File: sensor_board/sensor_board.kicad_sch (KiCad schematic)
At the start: 11 parts, among them J2 Conn_01x05_Pin, U2 LTC4316IMS-PBF

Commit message: sensor board
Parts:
- removed JP1, JP2: SolderJumper_2_Open, symbol Jumper:SolderJumper_2_Open
- removed R3: R_LT, symbol Device:R
- removed R4, R5, R6: R, symbol Device:R
- removed R7: R_HT, symbol Device:R
- removed U2: LTC4316IMS-PBF, MSOP-10_MS_LIT, symbol LTC4316:LTC4316IMS-PBF
- added C3, C4: 0.1uF, symbol Device:C
- added C5: 10uF, symbol Device:C
- added RT2: NTCLE203E3103GB0, NTCLE203E3103GB0, symbol NTCLE203E3103GB0:NTCLE203E3103GB0
- added U1: TSL25911FN, SON-06-FN_2000X2400_AMS, symbol TSL25911:TSL25911FN
- R1: value R_LB -> 1k
- R2: value R_HB -> 5.6k
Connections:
- net +3V3: now also R1.2, C3.2, C4.2, C5.1, RT2.2, U1.5 (VDD)
- net GND: now also R2.2, C3.1, C5.2; no longer R1.1, R2.1
- net SCL: now also J2.5 (Pin_5), U1.1 (SCL)
- net SDA: now also J2.4 (Pin_4), U1.6 (SDA)
- net VOUT: now also R2.1, RT2.1
- new net: R1.1, U1.2 (INT)
- new net: C4.1, U1.3 (GND)

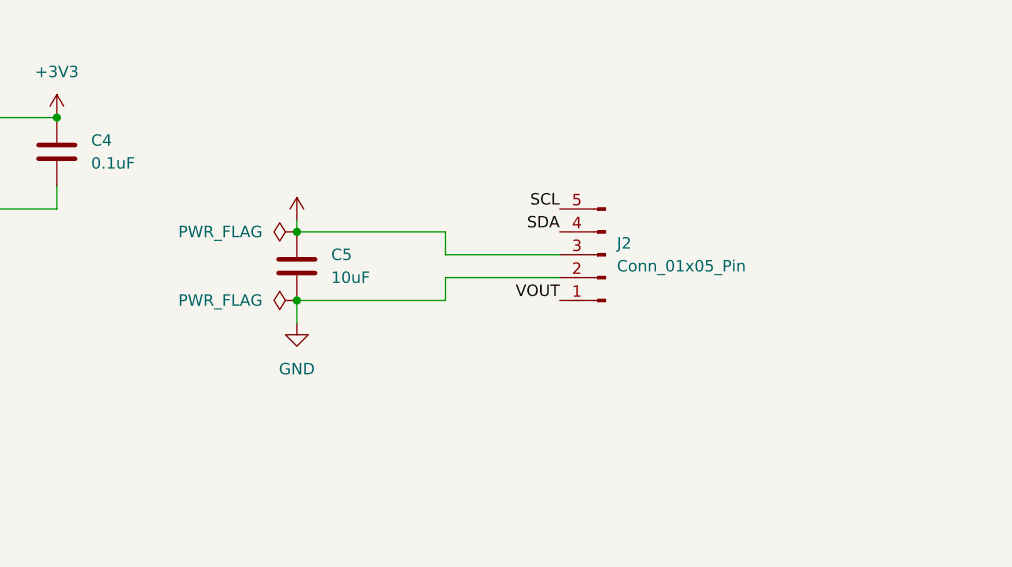
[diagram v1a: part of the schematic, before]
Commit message: added more complexity + thermistor connection
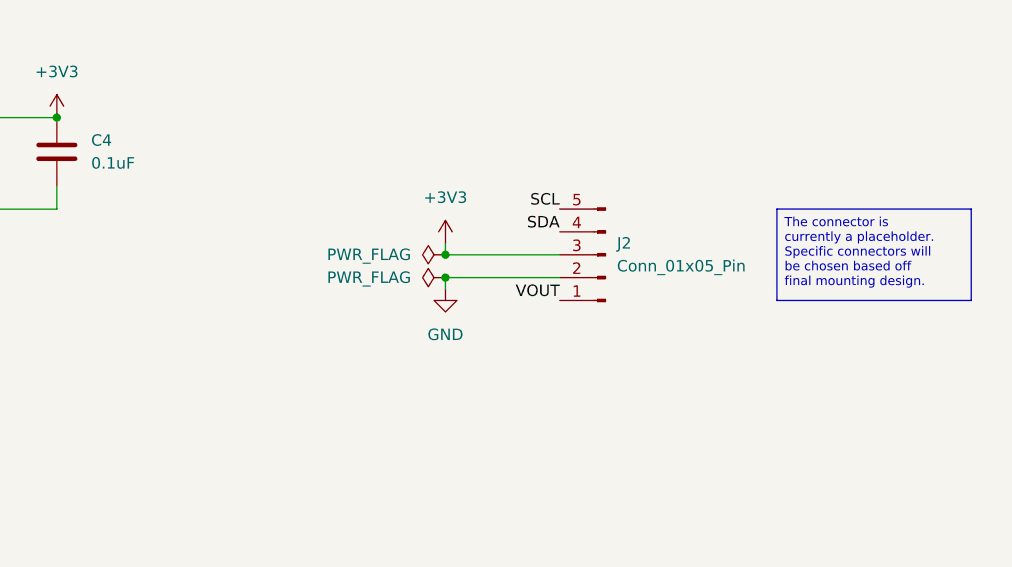
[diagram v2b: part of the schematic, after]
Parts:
- removed C5: 10uF, symbol Device:C

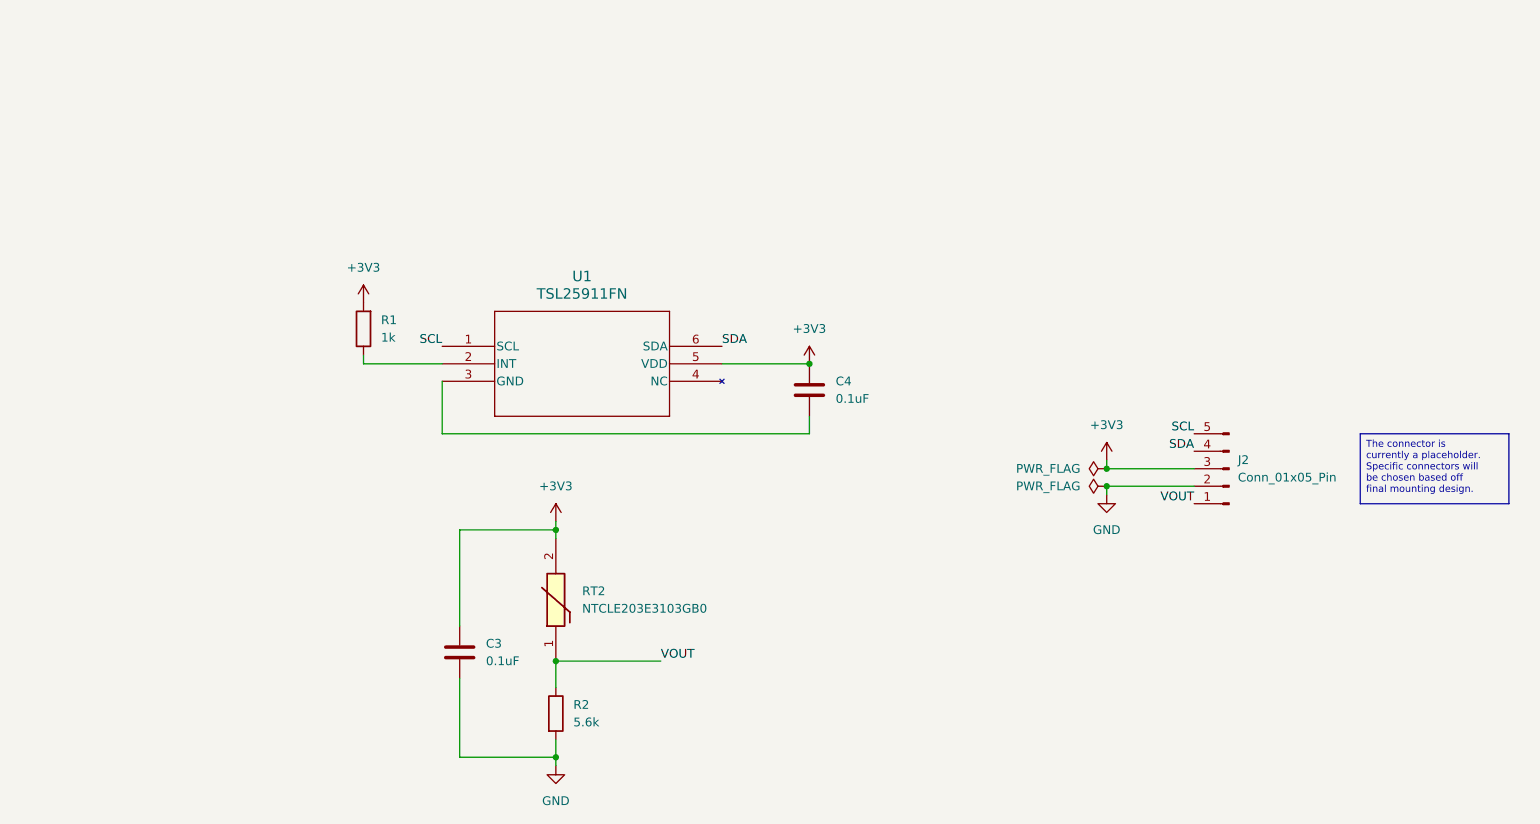
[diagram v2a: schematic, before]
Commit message: Initial version of sensor communication through all three boards
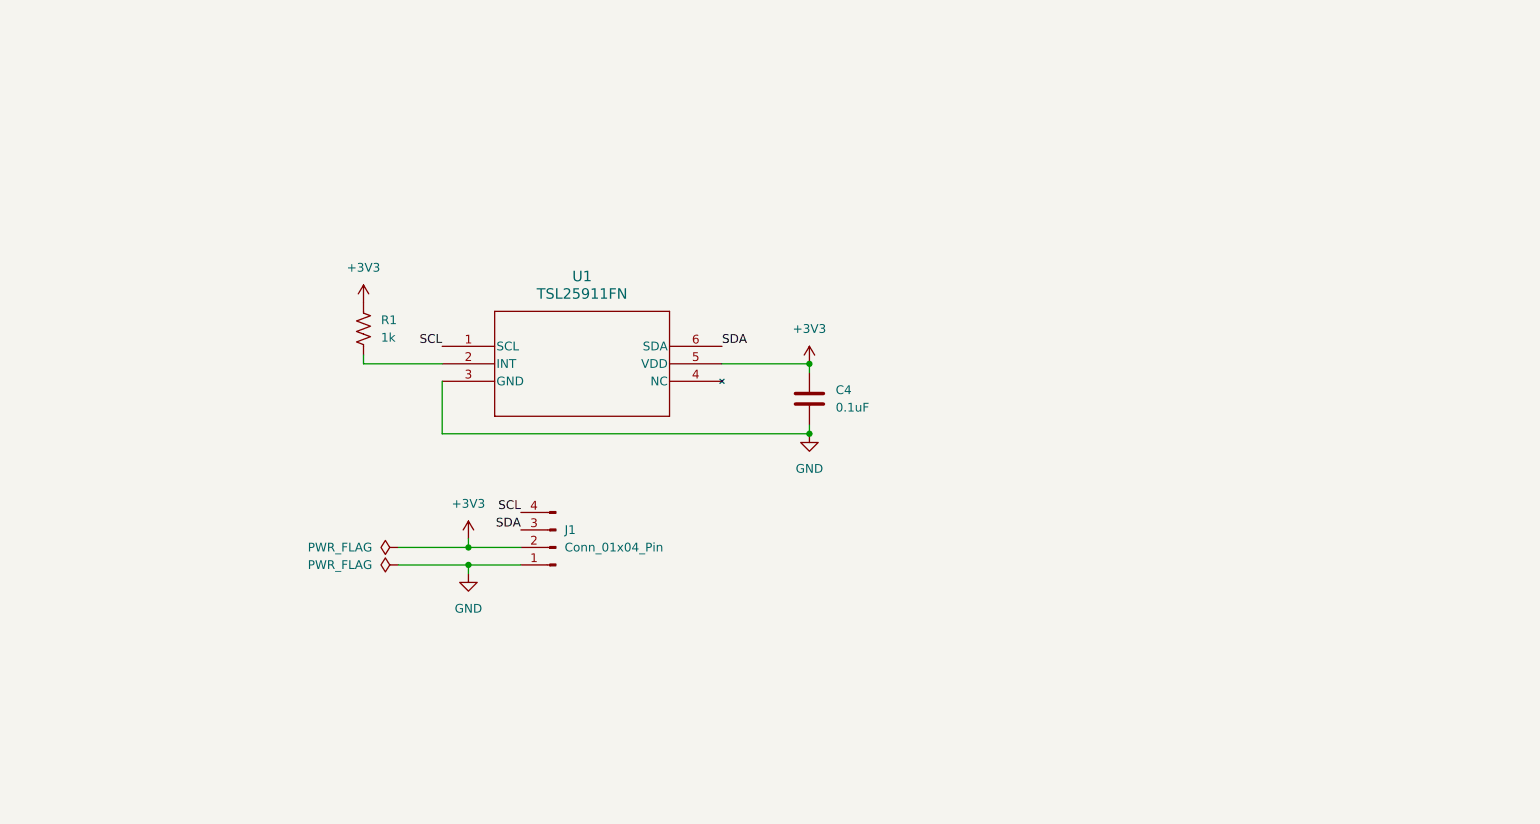
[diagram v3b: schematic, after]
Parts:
- removed C3: 0.1uF, symbol Device:C
- removed J2: Conn_01x05_Pin, symbol Connector:Conn_01x05_Pin
- removed R1: 1k, symbol Device:R
- removed R2: 5.6k, symbol Device:R
- removed RT2: NTCLE203E3103GB0, NTCLE203E3103GB0, symbol NTCLE203E3103GB0:NTCLE203E3103GB0
- added J1: Conn_01x04_Pin, symbol Connector:Conn_01x04_Pin
- added R1: 1k, symbol Device:R_US
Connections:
- net +3V3: now also J1.2 (Pin_2), R1.1
- net GND: now also C4.1, U1.3 (GND), J1.1 (Pin_1)
- net SCL: now also J1.4 (Pin_4)
- net SDA: now also J1.3 (Pin_3)
- net at U1.2 (INT): now also R1.2
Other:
- moved on the sheet: C4

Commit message: Updated minor errors
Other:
- moved on the sheet: C4
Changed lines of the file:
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@@
 	)
 	(junction
-		(at 152.4 100.33)
+		(at 152.4 99.06)
 		(diameter 0)
 		(color 0 0 0 0)
@@
 	(wire
 		(pts
-			(xy 99.06 100.33) (xy 152.4 100.33)
+			(xy 99.06 99.06) (xy 152.4 99.06)
 		)
 		(stroke
@@
 	(wire
 		(pts
-			(xy 99.06 92.71) (xy 99.06 100.33)
-		)
-		(stroke
-			(width 0)
-			(type default)
-		)
-	)
-	(wire
-		(pts
-			(xy 152.4 91.44) (xy 152.4 90.17)
+			(xy 99.06 92.71) (xy 99.06 99.06)
 		)
 		(stroke
@@
 		(pts
 			(xy 102.87 116.84) (xy 110.49 116.84)
+		)
+		(stroke
+			(width 0)
+			(type default)
+		)
+	)
+	(wire
+		(pts
+			(xy 152.4 97.79) (xy 152.4 99.06)
 		)
 		(stroke
@@
 	(symbol
 		(lib_id "Device:C")
-		(at 152.4 95.25 180)
+		(at 152.4 93.98 180)
 		(unit 1)
 		(exclude_from_sim no)
@@
 		(fields_autoplaced yes)
 		(property "Reference" "C4"
-			(at 156.21 93.9799 0)
+			(at 156.21 92.7099 0)
 			(effects
 				(font
@@
 		)
 		(property "Value" "0.1uF"
-			(at 156.21 96.5199 0)
+			(at 156.21 95.2499 0)
 			(effects
 				(font
@@
 		)
 		(property "Footprint" ""
-			(at 151.4348 91.44 0)
+			(at 151.4348 90.17 0)
 			(effects
 				(font
@@
 		)
 		(property "Datasheet" "~"
-			(at 152.4 95.25 0)
+			(at 152.4 93.98 0)
 			(effects
 				(font
@@
 		)
 		(property "Description" "Unpolarized capacitor"
-			(at 152.4 95.25 0)
+			(at 152.4 93.98 0)
 			(effects
 				(font
@@
 			)
 		)
-		(property "Datasheet" "TSL25911FN"
+		(property "Datasheet" "https://cdn-shop.adafruit.com/datasheets/TSL25911_Datasheet_EN_v1.pdf"
 			(at 99.06 87.63 0)
 			(effects
